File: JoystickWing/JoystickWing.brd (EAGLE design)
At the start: 32.7 x 69.8 mm, 21 parts, among them J1 5747844-4

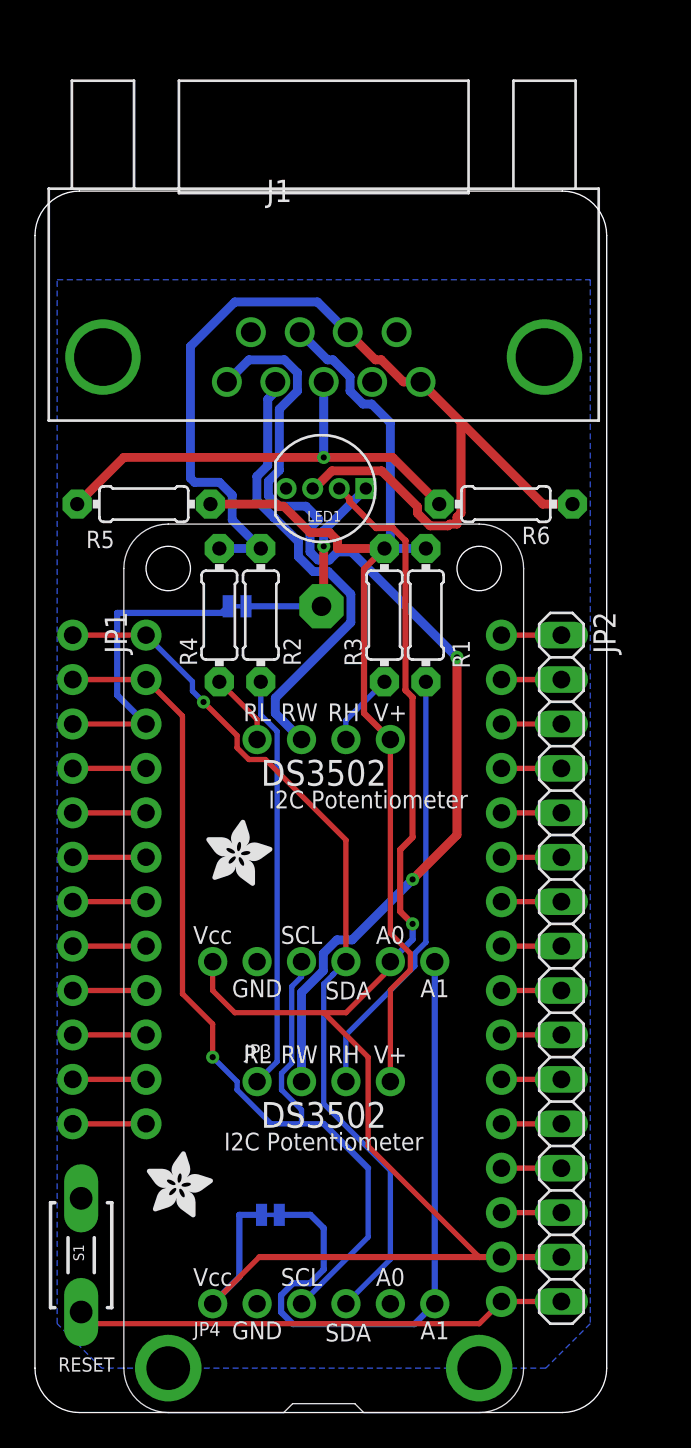
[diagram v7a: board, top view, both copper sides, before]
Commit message: Cleaning up for manu
Added restriction around traces for the jumpers
Added text and a place for the PCBWay product num
Replaced pins to be consistent
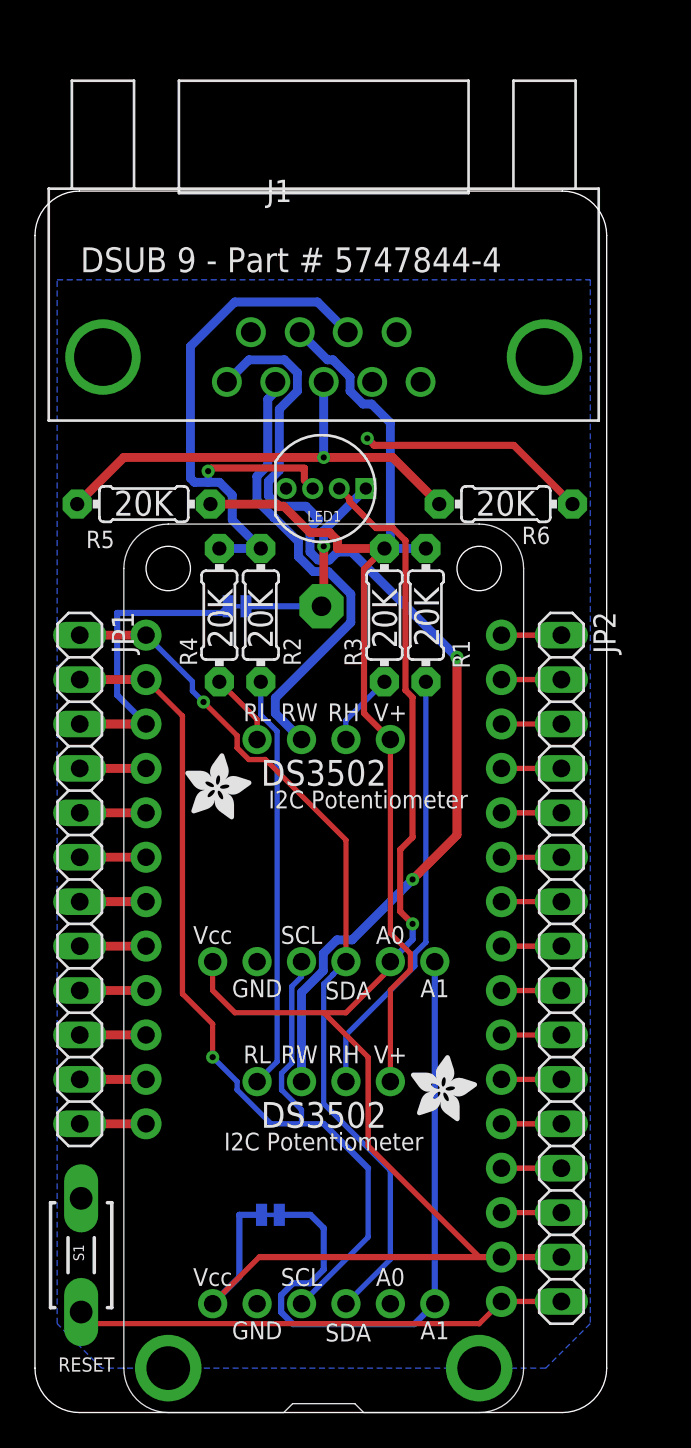
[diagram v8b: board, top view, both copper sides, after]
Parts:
- JP1: device adafruit:1X12-CB -> adafruit:1X12
- moved U$10 16.1 mm to (21.5, 16.6)
- moved U$11 3.98 mm to (8.58, 33.9)
- moved JP1 0.40 mm to (2.56, 30.5)
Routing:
- net GND: track 63.6 -> 51.4 mm, vias 0 -> 2
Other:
- board text added: "20K"
- board text added: "ATMakers"
- board text added: "DSUB 9 - Part # 5747844-4"
- board text added: "Product #"
